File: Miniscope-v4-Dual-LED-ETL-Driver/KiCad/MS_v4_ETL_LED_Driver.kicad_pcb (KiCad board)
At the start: 6 copper layers, 9.5 x 10.5 mm, 32 parts, among them J1 Conn_01x01, J10 Conn_01x05, J6 Conn_01x01, J7 Conn_01x01, U1 MAX14574EWL+, U2 TPL0102-100RUCR, U3 LTC3218, U4 LTC3218

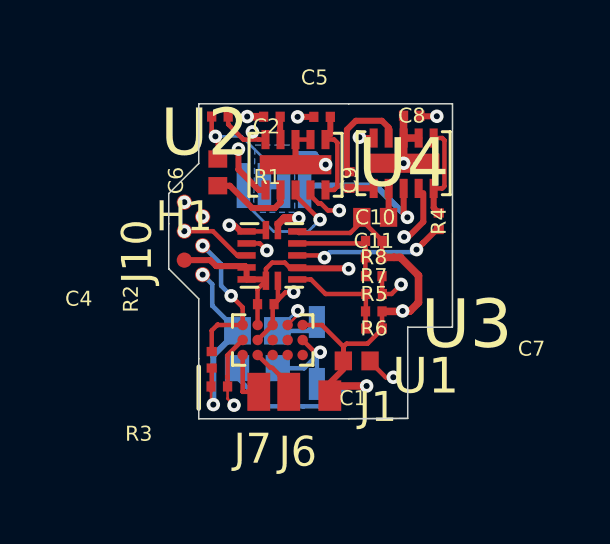
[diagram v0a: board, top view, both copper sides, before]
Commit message: Corrections
Fixed errors:

* Overlapping courtyards
* Traces very close to pads
* Bypass capacitors closer to pads
* Some courtyards (resistors/capacitors) had an error with the crosshairs. While not an important error it was fixed for easier debugging.
* Changed the symbol in the schematics for more consistency
To do

* Check the position of the LEDs relative to the miniscope
* Pour polygons planes in the LED ground pads
* Change the 3V3 and GND layer order
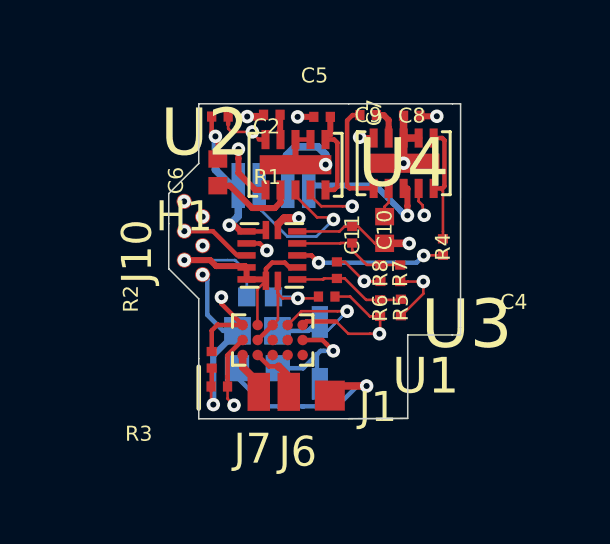
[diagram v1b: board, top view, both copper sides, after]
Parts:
- C1: moved to B.Cu
- moved C1 3.86 mm to (15.3, 19.7)
- moved C9 2.25 mm to (18.9, 13.7), turned to 180 degrees
- moved C4 2.05 mm to (17.6, 19.7), turned to 0 degrees
- moved C7 1.84 mm to (17.9, 18.8), turned to 90 degrees
- moved R5 1.00 mm to (20.0, 20.1), turned to 90 degrees
- moved R7 0.89 mm to (20.0, 18.9), turned to 90 degrees
- moved R4 0.87 mm to (21.4, 18.1)
- moved C11 0.75 mm to (18.4, 17.6), turned to 90 degrees
- moved R6 0.71 mm to (19.3, 20.1), turned to 270 degrees
- moved R8 0.57 mm to (19.3, 18.9), turned to 270 degrees
- moved C10 0.52 mm to (19.5, 17.5), turned to 270 degrees
- moved D2 0.17 mm to (14.9, 16.0), turned to 180 degrees
- moved D3 0.13 mm to (16.6, 16.0)
- moved D1 0.10 mm to (17.3, 21.6)
- moved C5 0.07 mm to (15.7, 13.7)
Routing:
- net Net-(D1-PadA): track 3.02 -> 6.21 mm
- net Net-(C9-Pad2): track 0.81 -> 3.60 mm
- net Net-(C9-Pad1): track 3.40 -> 1.08 mm
- net GND: track 42.3 -> 43.8 mm, vias 7 -> 9
- net +3V3: track 16.9 -> 18.1 mm, vias 8 -> 7
- net Net-(R4-Pad2): track 3.20 -> 4.25 mm
- net Net-(C3-Pad1): track 3.49 -> 4.26 mm
- net /ENT1: track 6.11 -> 6.85 mm
- removed copper zone on B.Cu, net GND
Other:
- board size 9.5 x 10.5 mm -> 9.7 x 10.5 mm
